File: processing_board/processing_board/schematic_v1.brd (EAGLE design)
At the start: 126 x 72 mm, 74 parts, among them J5 FEMALE 2x3, Q1 BSS138, Q2 BSS138, Q3 BSS138, Q4 BSS138, U1 SN74ALS166D

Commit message: updated board
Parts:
- moved R8 54.8 mm to (104.1, 16.0)
- moved C5 54.8 mm to (104.1, 18.8)
- moved C6 54.8 mm to (100.2, 18.8)
- moved D4 54.8 mm to (100.3, 16.0)
- moved U$3 54.8 mm to (102.1, 25.5)
- moved D1 48.0 mm to (84.2, 45.1)
- moved U$2 48.0 mm to (86.1, 53.4)
- moved C1 48.0 mm to (84.3, 47.4)
- moved C4 48.0 mm to (88.1, 47.4)
- moved R6 48.0 mm to (88.1, 45.1)
- moved R13 19.0 mm to (51.0, 47.4)
- moved D2 19.0 mm to (47.1, 43.4)
- moved D5 19.0 mm to (47.1, 47.4)
- moved D8 19.0 mm to (47.1, 45.3)
- moved R17 19.0 mm to (50.9, 45.4)
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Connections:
- removed net 3P3_1: S1.10, S1.11, S1.12, S1.13, S1.14, S1.15, S1.16, S1.9, U$4.3V3-3
- new net N$19: B1.GND@1
- net +5V: no longer B1.VIN, U1.16, U1.9
- net GND: no longer B1.GND@1
- net TEENSY_3.3V: now also S1.10, S1.11, S1.12, S1.13, S1.14, S1.15, S1.16, S1.9, U$4.3V3-1, U$4.3V3-2, U$4.3V3-3, U1.16, U1.9

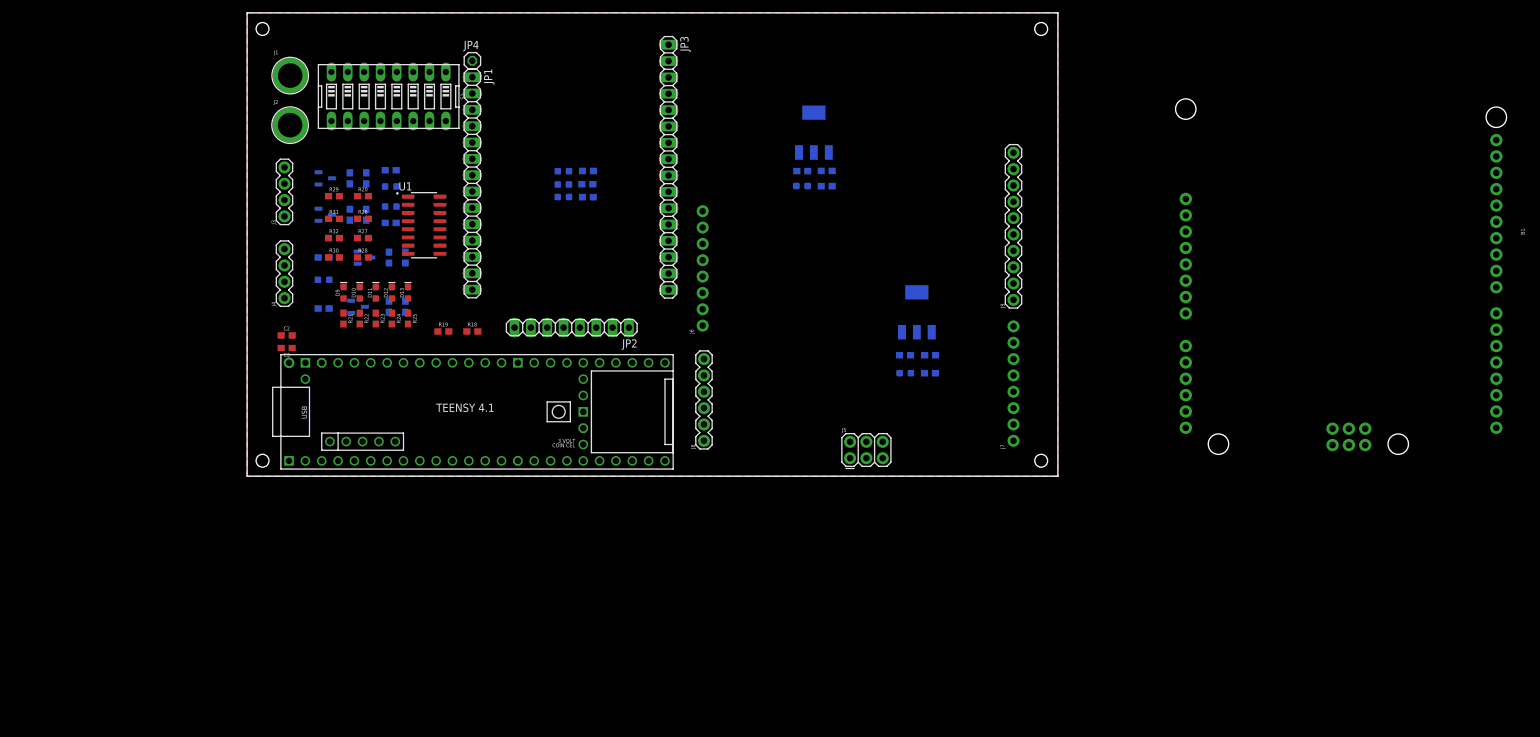
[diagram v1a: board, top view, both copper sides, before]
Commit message: added arduino
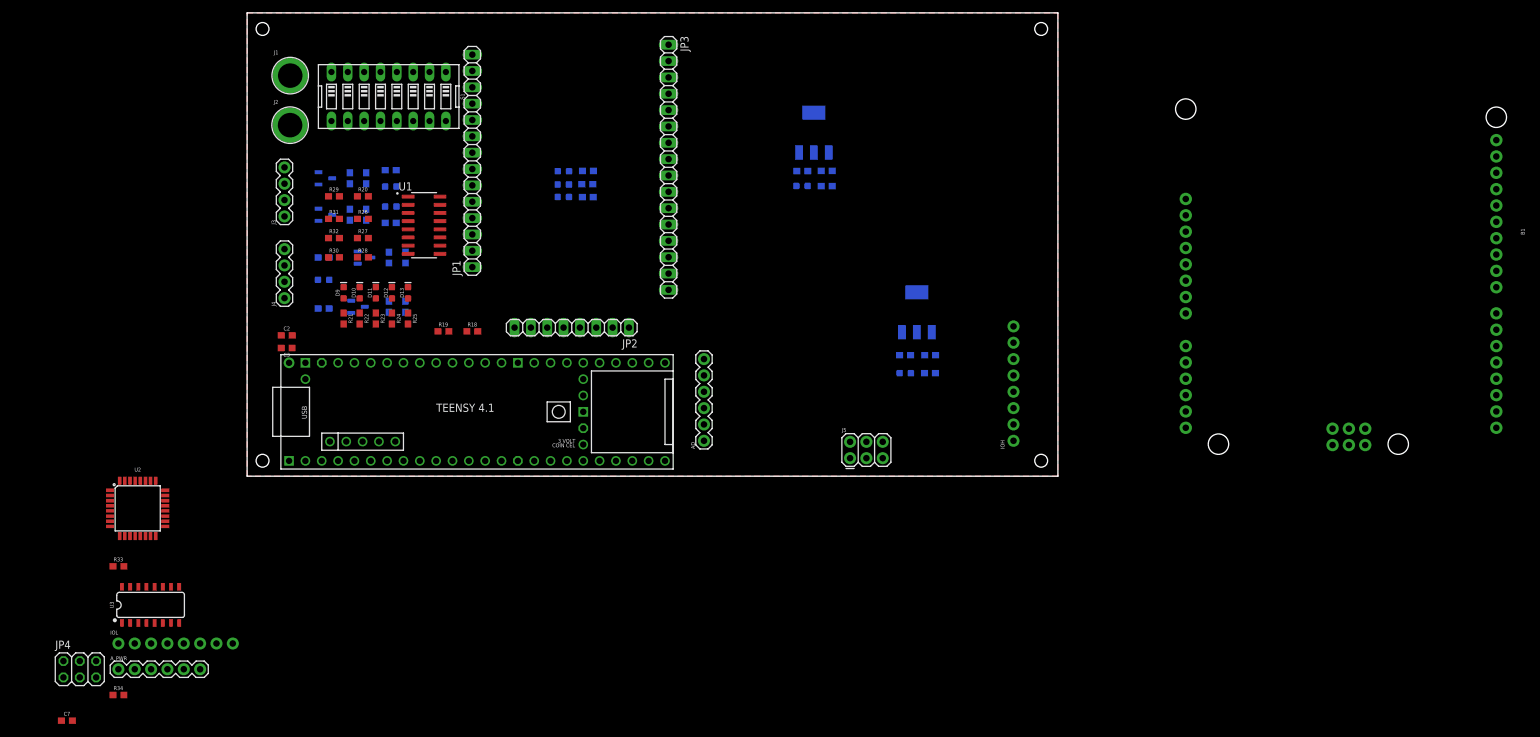
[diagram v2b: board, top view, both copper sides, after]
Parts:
- removed J6: (no value), SparkFun-Connectors:1X08_NO_SILK
- removed J9: (no value), SparkFun-Connectors:1X10
- added A_PWR: (no value), SparkFun-Connectors:1X06
- added C7: 0.1uF, SparkFun-Capacitors:0603
- added IOL: (no value), SparkFun-Connectors:1X08_NO_SILK
- added R33: 1k, SparkFun-Resistors:0603
- added R34: 10k, SparkFun-Resistors:0603
- added U2: ATMEGA328P_TQFP, SparkFun-IC-Microcontroller:TQFP32-08
- added U3: SN74HC595D, SparkFun-IC-Logic:SO16
- JP4: device pinhead:1X01 -> pinhead:2X03
- moved JP4 112.5 mm to (-28.0, -30.0)
- moved JP1 3.50 mm to (33.0, 49.0), turned to 90 degrees
- renumbered J7 to IOH, J8 to AD
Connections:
- net CAN_RX1 renamed SDA_BUS
- net CAN_TX1 renamed SCL_BUS
- new net A_AREF: IOH.8, U2.20
- new net A_MISO: IOH.5, JP4.1, U2.16
- new net A_MOSI: IOH.4, JP4.4, U2.15
- new net A_RESET: A_PWR.1, JP4.5, R34.2, U2.29
- new net A_SCK: IOH.6, JP4.3, U2.17
- new net A_SS: IOH.3, U2.14
- new net N$26: JP1.11, U$4.33-MCLK2
- new net N$27: R33.1, U1.9
- new net N$28: AD.1, U2.23
- new net N$29: AD.2, U2.24
- new net N$31: AD.3, U2.25
- new net N$32: AD.4, U2.26
- new net N$33: AD.5, U2.27
- new net N$34: AD.6, U2.28
- new net N$35: IOH.2, U2.13
- new net N$36: IOH.1, U2.12
- new net N$37: IOL.8, U2.11
- new net N$38: IOL.7, U2.10
- new net N$39: IOL.6, U2.9
- new net N$40: IOL.5, U2.2
- new net N$41: IOL.4, U2.1
- new net N$42: IOL.3, U2.32
- new net N$43: IOL.2, U2.31
- new net N$44: IOL.1, U2.30
- new net N$50: A_PWR.6
- new net VCC: U3.16
- net +3.3V: now also A_PWR.2, JP1.3; no longer JP1.2
- net +5V: now also A_PWR.3, C7.1, JP4.2, R34.1, U2.18, U2.4, U2.6; no longer J6.1
- net GND: now also A_PWR.4, A_PWR.5, C7.2, IOH.7, JP1.12, JP1.14, JP1.2, JP4.6, U2.21, U2.3, U2.5, U3.8; no longer J6.2, J6.3, JP1.11, JP1.13, JP4.1
- net N$1: now also JP1.5; no longer JP1.4
- net N$2: now also JP1.4; no longer JP1.3
- net N$3: now also JP1.13; no longer JP1.12
- net RESET_: now also JP1.7; no longer JP1.10, JP1.6, U$4.33-MCLK2
- net TEENSY_3.3V: now also R33.2; no longer U1.9

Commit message: updated board
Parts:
- removed J1, J2: (no value), SparkFun-Connectors:BANANA_CONN
- removed U3: SN74HC595D, SparkFun-IC-Logic:SO16
- added BT1: (no value), SparkFun-Batteries:BATTCON_20MM
- added Y1: 16MHz, SparkFun-Clocks:RESONATOR-SMD-3.2X1.3
- J5: value FEMALE 2x3 -> (none); device SparkFun-Connectors:2X3 -> SparkFun-Connectors:1X02_LOCK_LONGPADS
- moved IOL 142.6 mm to (117.1, 5.50), turned to 90 degrees
- moved C7 137.4 mm to (87.0, 34.0), turned to 90 degrees
- moved JP4 126.9 mm to (94.2, 4.10), turned to 180 degrees
- moved R34 126.8 mm to (85.0, 34.0), turned to 90 degrees
- moved A_PWR 112.3 mm to (68.9, 35.9), turned to 270 degrees
- moved U2 108.5 mm to (85.0, 26.0), turned to 90 degrees
- moved J5 107.5 mm to (2.00, 62.0), turned to 270 degrees
- moved R33 67.3 mm to (28.0, 31.0), turned to 270 degrees
- moved U$3 28.3 mm to (98.1, 53.5)
- moved C5 28.3 mm to (100.1, 46.8)
- moved C6 28.3 mm to (96.2, 46.8)
- moved D4 28.3 mm to (96.3, 44.0)
- moved R8 28.3 mm to (100.1, 44.0)
- moved IOH 21.8 mm to (117.1, 27.3)
- moved AD 12.6 mm to (68.9, 18.1), turned to 270 degrees
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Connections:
- net N$28 renamed A_A0
- net N$44 renamed RXD
- removed net N$34: AD.6, U2.28
- removed net VCC: U3.16
- new net N$45: U2.7, Y1.1
- new net N$46: U2.8, Y1.3
- net +15V: now also J5.1; no longer J1.P$1
- net GND: now also BT1.2, J5.2, Y1.2; no longer J2.P$1, U3.8
- net N$33: now also BT1.1, U$4.VBAT; no longer AD.5, U2.27
- net SCL_BUS: now also AD.6, U2.28
- net SDA_BUS: now also AD.5, U2.27
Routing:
- net GND: track 0.00 -> 523.1 mm, vias 0 -> 2
- net +5V: track 0.00 -> 315.7 mm, vias 0 -> 6
- net TEENSY_3.3V: track 0.00 -> 198.3 mm, vias 0 -> 3
- net SCL_BUS: track 0.00 -> 126.0 mm, vias 0 -> 4
- net +15V: track 0.00 -> 125.0 mm, vias 0 -> 2
- net SDA_BUS: track 0.00 -> 123.5 mm, vias 0 -> 3
- net +3.3V: track 0.00 -> 117.8 mm, vias 0 -> 1
- net N$33: track 0.00 -> 90.4 mm
- net N$9: track 0.00 -> 84.1 mm
- net RXD: track 0.00 -> 80.4 mm, vias 0 -> 1
- net A_SCK: track 0.00 -> 77.4 mm
- net N$42: track 0.00 -> 75.5 mm
- net A_MISO: track 0.00 -> 73.2 mm
- net A_MOSI: track 0.00 -> 72.3 mm
- net N$41: track 0.00 -> 69.7 mm
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- removed copper zone on layer 1, net GND
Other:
- board text added: "5 TX RX GND"
- board text added: "CAN"
- board text added: "FREQ_SET"
- board text added: "GND"
- board text added: "GND 5 SDA SCL"
- board text added: "PWR"

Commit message: finished wiring
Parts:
- removed JP2: (no value), pinhead:1X08
- moved JP1 3.50 mm to (33.0, 45.5), turned to 270 degrees
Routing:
- net +15V: track 125.0 -> 193.8 mm, vias 2 -> 1
- net N$41: track 69.7 -> 39.5 mm
- net TEENSY_3.3V: track 198.3 -> 171.9 mm
- net GND: track 523.1 -> 496.9 mm, vias 2 -> 3
- net +3.3V: track 117.8 -> 143.5 mm, vias 1 -> 4
- net +5V: track 315.7 -> 292.3 mm, vias 6 -> 7
- net RXD: track 80.4 -> 57.0 mm
- net N$9: track 84.1 -> 61.5 mm
- net D: track 45.6 -> 66.3 mm, vias 0 -> 1
- net N$2: track 55.8 -> 76.3 mm
- net N$26: track 57.8 -> 37.8 mm
- net H: track 59.3 -> 42.8 mm, vias 1 -> 2
- net N$32: track 38.4 -> 24.3 mm
- net SDA_BUS: track 123.5 -> 111.2 mm, vias 3 -> 5
- net N$11: track 49.3 -> 58.7 mm
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- added copper zone on layer 1, net GND
- added copper zone on layer 16, net GND

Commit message: generated gerber files
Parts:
- removed B1: ARDUINO_UNO_R3, SparkFun-Boards:ARDUINO_R3
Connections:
- removed net N$19: B1.GND@1
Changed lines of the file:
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@@
 </element>
 <element name="U$4" library="teensy" package="TENNSY41-E" value="TEENSY41-E" x="35" y="10" smashed="yes"/>
-<element name="B1" library="SparkFun-Boards" package="ARDUINO_R3" value="ARDUINO_UNO_R3" x="163" y="38" smashed="yes" rot="R270">
-<attribute name="NAME" x="190.94" y="38" size="0.6096" layer="25" font="vector" ratio="20" rot="R270" align="bottom-center"/>
-<attribute name="VALUE" x="131.06" y="40" size="0.6096" layer="27" font="vector" ratio="20" rot="R270" align="top-center"/>
-</element>
 <element name="R18" library="SparkFun-Resistors" package="0603" value="10k" x="33" y="22.5" smashed="yes">
 <attribute name="NAME" x="33" y="23.262" size="0.6096" layer="25" font="vector" ratio="20" align="bottom-center"/>
@@
 <via x="29.8704" y="29.8704" extent="1-16" drill="0.35"/>
 </signal>
-<signal name="N$19">
-<contactref element="B1" pad="GND@1"/>
-</signal>
 <signal name="N$26">

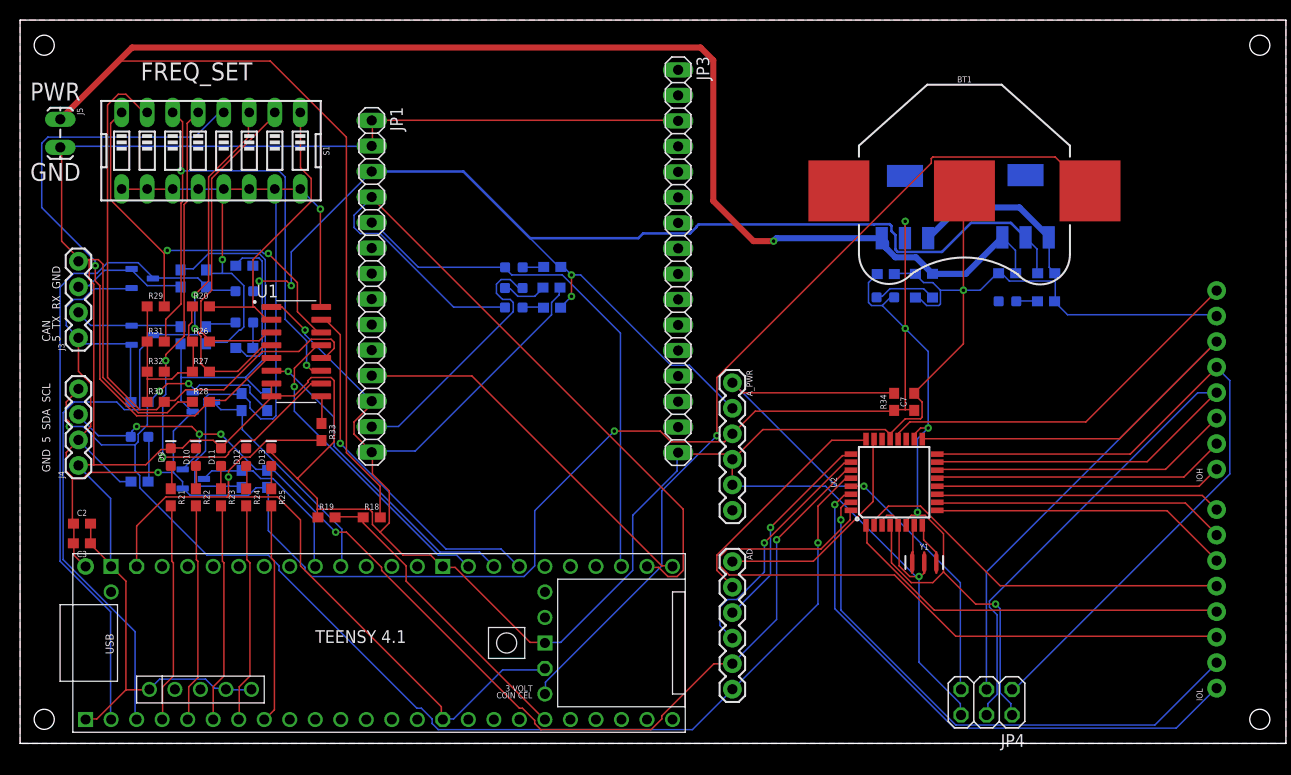
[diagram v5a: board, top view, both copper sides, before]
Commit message: updated shif register
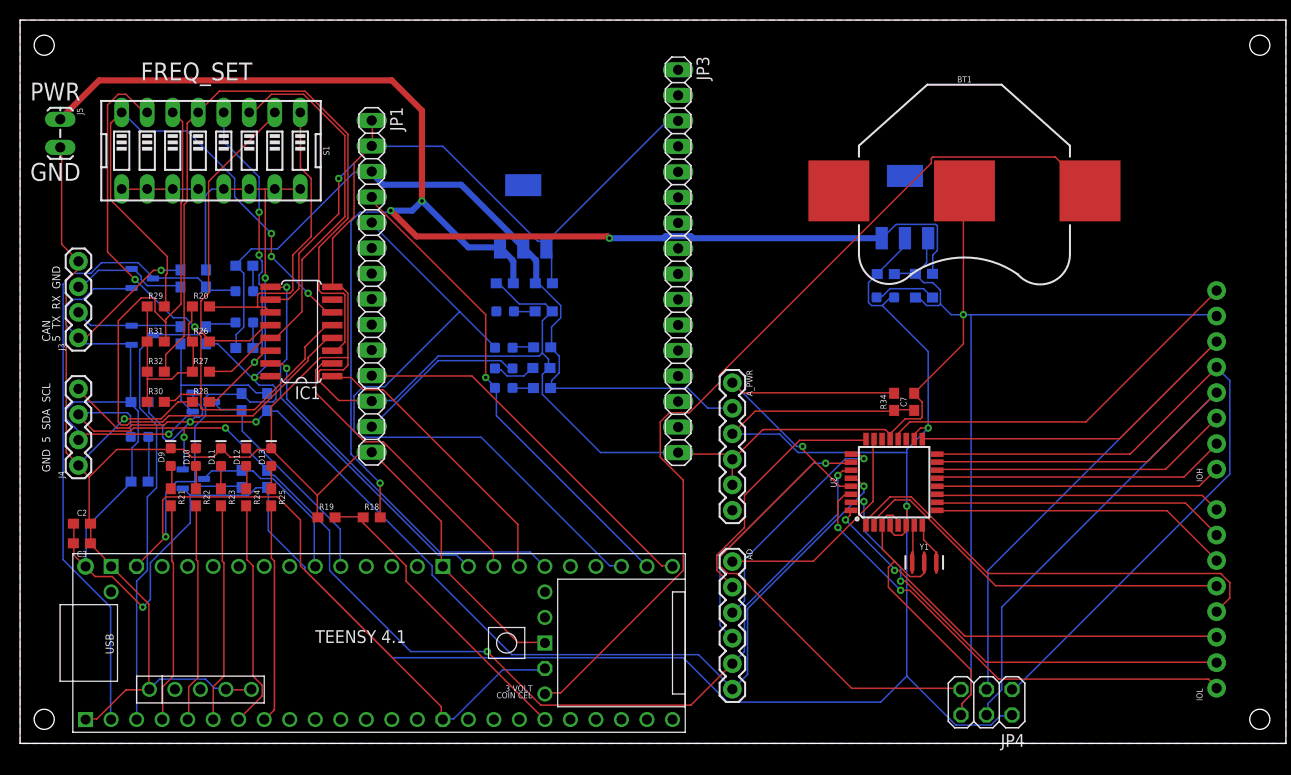
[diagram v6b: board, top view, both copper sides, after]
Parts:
- removed R33: 1k, SparkFun-Resistors:0603
- removed U1: SN74ALS166D, SN74ALS166D - TI level shifter:SOIC127P600X175-16N
- added IC1: 74HC165D, 74xx-eu:SO16
- moved R8 50.0 mm to (50.1, 43.0)
- moved C5 50.0 mm to (50.1, 45.8)
- moved C6 50.0 mm to (46.2, 45.8)
- moved D4 50.0 mm to (46.3, 43.0)
- moved U$3 50.0 mm to (48.1, 52.5)
- moved D2 8.06 mm to (46.1, 35.4)
- moved D5 8.06 mm to (46.1, 39.4)
- moved D8 8.06 mm to (46.1, 37.3)
- moved R13 8.06 mm to (50.0, 39.4)
- moved R17 8.06 mm to (49.9, 37.4)
- moved R5 8.06 mm to (50.0, 35.4)
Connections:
- removed net A: R20.2, S1.1, U1.2
- removed net C: R27.2, S1.3, U1.4
- removed net D: R28.2, S1.4, U1.5
- removed net E: R32.2, S1.5, U1.10
- removed net H: R29.2, S1.8, U1.14
- removed net N$25: R31.2, S1.6, U1.11
- removed net N$27: R33.1, U1.9
- removed net N$30: R26.2, S1.2, U1.3
- removed net N$9: R30.2, S1.7, U1.12
- removed net TEENSY_3.3V: R1.2, R12.2, R33.2, R4.2, R9.2, S1.10, S1.11, S1.12, S1.13, S1.14, S1.15, S1.16, S1.9, U$4.3V3-1, U$4.3V3-2, U$4.3V3-3, U1.16
- new net CLK_INH: IC1.15, U$4.38-A14/CS/IN1
- new net S_A: IC1.11, R20.2, S1.1
- new net S_B: IC1.12, R26.2, S1.2
- new net S_C: IC1.13, R27.2, S1.3
- new net S_D: IC1.14, R28.2, S1.4
- new net S_E: IC1.3, R32.2, S1.5
- new net S_F: IC1.4, R31.2, S1.6
- new net S_G: IC1.5, R30.2, S1.7
- new net S_H: IC1.6, R29.2, S1.8
- new net VCC: IC1.16, R1.2, R12.2, R4.2, R9.2, S1.10, S1.11, S1.12, S1.13, S1.14, S1.15, S1.16, S1.9, U$4.3V3-1, U$4.3V3-2, U$4.3V3-3
- net DIP_SW_SERIAL: now also IC1.9; no longer U1.13
- net GND: now also IC1.10, IC1.8; no longer U1.1, U1.7, U1.8
- net LS_CK: now also IC1.2; no longer U1.6
- net SH_LD: now also IC1.1; no longer U1.15
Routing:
- net TEENSY_3.3V: track 171.9 -> 0.00 mm, vias 3 -> 0
- net VCC: track 0.00 -> 147.9 mm, vias 0 -> 3
- net S_E: track 0.00 -> 70.7 mm
- net S_F: track 0.00 -> 66.7 mm
- net D: track 66.3 -> 0.00 mm, vias 1 -> 0
- net N$9: track 61.5 -> 0.00 mm
- net S_G: track 0.00 -> 61.2 mm, vias 0 -> 2
- net +3.3V: track 143.5 -> 84.8 mm, vias 4 -> 0
- net N$25: track 56.1 -> 0.00 mm, vias 2 -> 0
- net E: track 55.9 -> 0.00 mm, vias 2 -> 0
- net S_H: track 0.00 -> 53.9 mm, vias 0 -> 3
- net S_C: track 0.00 -> 43.0 mm
- net H: track 42.8 -> 0.00 mm, vias 2 -> 0
- net CLK_INH: track 0.00 -> 37.5 mm, vias 0 -> 1
- net C: track 36.0 -> 0.00 mm, vias 2 -> 0
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
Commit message: updated board
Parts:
- removed AD, A_PWR: (no value), SparkFun-Connectors:1X06
- removed BT1: (no value), SparkFun-Batteries:BATTCON_20MM
- removed C7: 0.1uF, SparkFun-Capacitors:0603
- removed IOH, IOL: (no value), SparkFun-Connectors:1X08_NO_SILK
- removed JP1: (no value), pinhead:1X14
- removed JP3: (no value), pinhead:1X16
- removed JP4: (no value), pinhead:2X03
- removed R34: 10k, SparkFun-Resistors:0603
- removed U2: ATMEGA328P_TQFP, SparkFun-IC-Microcontroller:TQFP32-08
- removed Y1: 16MHz, SparkFun-Clocks:RESONATOR-SMD-3.2X1.3
- added U$1: XBEE_SX_PRO, xbee_sx_pro:XBEE_SX_PRO
- moved R17 100.1 mm to (-36.0, -14.0), flipped to the top
- moved D8 99.9 mm to (-37.0, -18.0), flipped to the top
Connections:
- removed net A_A0: AD.1, U2.23
- removed net A_AREF: IOH.8, U2.20
- removed net A_MISO: IOH.5, JP4.1, U2.16
- removed net A_MOSI: IOH.4, JP4.4, U2.15
- removed net A_RESET: A_PWR.1, JP4.5, R34.2, U2.29
- removed net A_SCK: IOH.6, JP4.3, U2.17
- removed net A_SS: IOH.3, U2.14
- removed net N$1: D5.C, JP1.5, U$4.35-TX8
- removed net N$2: D2.C, JP1.4, U$4.34-RX8
- removed net N$26: JP1.11, U$4.33-MCLK2
- removed net N$29: AD.2, U2.24
- removed net N$3: D8.A, JP1.13
- removed net N$31: AD.3, U2.25
- removed net N$32: AD.4, U2.26
- removed net N$33: BT1.1, U$4.VBAT
- removed net N$35: IOH.2, U2.13
- removed net N$36: IOH.1, U2.12
- removed net N$37: IOL.8, U2.11
- removed net N$38: IOL.7, U2.10
- removed net N$39: IOL.6, U2.9
- removed net N$40: IOL.5, U2.2
- removed net N$41: IOL.4, U2.1
- removed net N$42: IOL.3, U2.32
- removed net N$43: IOL.2, U2.31
- removed net N$45: U2.7, Y1.1
- removed net N$46: U2.8, Y1.3
- removed net N$50: A_PWR.6
- removed net RESET_: JP1.7
- removed net RXD: IOL.1, U2.30
- new net DIN: D5.C, U$1.4, U$4.35-TX8
- new net DOUT: D2.C, U$1.3, U$4.34-RX8
- new net EXTRA: U$1.10, U$4.33-MCLK2
- new net N$12: D8.A, U$1.12
- new net RESET: U$1.6, U$4.32-OUT1B
- net +3.3V: now also U$1.2, U$4.3V3-1, U$4.3V3-2, U$4.3V3-3; no longer A_PWR.2, JP1.3
- net +5V: now also U$4.+5V; no longer A_PWR.3, C7.1, JP4.2, R34.1, U2.18, U2.4, U2.6
- net GND: now also U$1.1, U$1.11, U$1.13, U$1.22, U$1.35, U$1.38; no longer A_PWR.4, A_PWR.5, BT1.2, C7.2, IOH.7, JP1.1, JP1.12, JP1.14, JP1.2, JP3.16, JP3.3, JP4.6, U$4.+5V, U2.21, U2.3, U2.5, Y1.2
- net SCL_BUS: no longer AD.6, U2.28
- net SDA_BUS: no longer AD.5, U2.27
- net VCC: no longer U$4.3V3-1, U$4.3V3-2, U$4.3V3-3
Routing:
- net N$33: track 90.4 -> 0.00 mm
- net GND: track 490.2 -> 404.1 mm
- net A_SCK: track 77.4 -> 0.00 mm
- net A_RESET: track 76.1 -> 0.00 mm, vias 1 -> 0
- net A_MISO: track 73.2 -> 0.00 mm
- net A_MOSI: track 72.3 -> 0.00 mm
- net N$1: track 67.3 -> 0.00 mm
- net DIN: track 0.00 -> 67.2 mm
- net RXD: track 48.6 -> 0.00 mm, vias 2 -> 0
- net N$2: track 48.2 -> 0.00 mm, vias 1 -> 0
- net DOUT: track 0.00 -> 48.0 mm, vias 0 -> 1
- net N$43: track 45.6 -> 0.00 mm, vias 2 -> 0
- net N$41: track 44.6 -> 0.00 mm
- net N$42: track 43.1 -> 0.00 mm, vias 2 -> 0
- net N$40: track 39.0 -> 0.00 mm
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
